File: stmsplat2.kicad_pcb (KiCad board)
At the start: 2 copper layers, 100 x 100 mm, 115 parts, among them J1 C11_2X36, J10 Conn_01x03_Male, J11 Conn_01x02_Male, J12 Conn_01x04_Male, J13 Conn_01x04_Male, J14 Conn_01x02, J15 Conn_01x02, J16 Screw_Terminal_01x03, J17 Screw_Terminal_01x02, J18 Conn_01x02_Male, J19 Conn_01x02_Male, J2 C12_2X36, J3 Conn_01x04_Male, J4 Conn_01x04_Male, J5 Conn_Coaxial, J6 Conn_01x04_Male, J7 Conn_01x04_Male, J8 Conn_01x04_Male, J9 Conn_01x03_Male, Q1 BSS138LT1G, SW1 SW_DIP_x02, U1 ublox_chinese_PCB_module, U10 XCVR_E30-400M20S (Si4463), U11 3115_module, U2 ESP-C3-13U, U3 SST25VF032B, U4 48L512-48LM01, U5 Opamp_Quad_MCP6024, U6 E180-ZG120A, U7 AZ1084C, U8 MCP6S93-X_UN, U9 DS2485

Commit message: Splat2 Revision A.  Work-in-progress
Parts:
- J1, J2: footprint Connector_Samtec_HLE_THT:Samtec_HLE-136-02-xx-DV-TE_2x36_P2.54mm_Horizontal -> Connector_PinSocket_2.54mm:PinSocket_2x36_P2.54mm_Vertical
- R7, R8: value 4K7 -> 1K
- moved TP10 2.07 mm to (149.8, 140.0)
- turned J1 to 180 degrees
- turned J2 to 180 degrees
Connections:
- net Net-(C13-Pad1) renamed /OUR3V3
- C1 pad 1: VDD -> +3V3
- C11 pad 1: +5V -> 5VEXT
- C14 pad 2: VDD -> +3V3
- C15 pad 1: VDD -> +3V3
- C16 pad 2: VDD -> +3V3
- C17 pad 2: VDD -> +3V3
- C18 pad 1: VDD -> +3V3
- C19 pad 2: VDD -> +3V3
- C2 pad 1: VDD -> +3V3
- C20 pad 1: VDD -> +3V3
- C21 pad 2: VDD -> +3V3
- C28 pad 1: VDD -> +3V3
- C3 pad 1: VDD -> +3V3
- C30 pad 1: VDD -> +3V3
- C31 pad 1: VDD -> +3V3
- FB1 pad 2: +5V -> 5VEXT
- FB2 pad 1: VDD -> +3V3
- J1 pad 16: /+3V3 -> +3V3
- J1 pad 18: +5V -> +5VSTM
- J1 pad 5: VDD -> /3V3_VPP
- J1 pad 57: /PD0 -> PD0
- J1 pad 6: +5V -> 5VEXT
- J12 pad 1: VDD -> +3V3
- J13 pad 1: VDD -> +3V3
- J19 pad 2: VDD -> +3V3
- J4 pad 1: VDD -> +3V3
- J7 pad 1: VDD -> +3V3
- Q1 pad 3: VDD -> +3V3
- R1 pad 1: VDD -> +3V3
- R10 pad 2: GNDA -> /HALF3V3
- R11 pad 1: VDD -> +3V3
- R13 pad 1: VDD -> +3V3
- R14 pad 1: VDD -> +3V3
- R16 pad 2: VDD -> +3V3
- R21 pad 1: VDD -> +3V3
- R22 pad 1: VDD -> +3V3
- R4 pad 1: VDD -> +3V3
- U1 pad 1: VDD -> +3V3
- U10 pad 9: VDD -> +3V3
- U11 pad 1: PB9 -> PD0
- U11 pad 5: VDD -> +3V3
- U2 pad 1: VDD -> +3V3
- U3 pad 8: VDD -> +3V3
- U4 pad 8: VDD -> +3V3
- U6 pad 3: VDD -> +3V3
- U7 pad 3: +5V -> 5VEXT
- U9 pad 6: VDD -> +3V3
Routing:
- net +3V3: track 0.00 -> 574.4 mm, vias 0 -> 8
- net VDD: track 569.9 -> 0.00 mm, vias 8 -> 0
- net PA4: track 153.4 -> 0.00 mm, vias 3 -> 0
- net PE6: track 131.7 -> 0.00 mm, vias 5 -> 0
- net PC10: track 125.1 -> 0.00 mm, vias 6 -> 0
- net PA0: track 126.4 -> 8.97 mm, vias 2 -> 1
- net PD11: track 115.9 -> 0.00 mm, vias 3 -> 0
- net PC6: track 115.7 -> 0.00 mm, vias 1 -> 0
- net PE1: track 115.0 -> 0.00 mm, vias 1 -> 0
- net PE2: track 114.8 -> 0.00 mm, vias 5 -> 0
- net PB9: track 109.7 -> 0.00 mm, vias 3 -> 0
- net PE13: track 109.0 -> 0.00 mm, vias 4 -> 0
- net PG9: track 107.6 -> 0.00 mm, vias 2 -> 0
- net PF2: track 100.8 -> 0.00 mm, vias 3 -> 0
- net PG2: track 99.4 -> 0.00 mm, vias 3 -> 0
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- removed copper zone on B.Cu, net GND
- removed copper zone on B.Cu, net GNDA
- removed copper zone on F.Cu, net GNDA
- removed copper zone on F.Cu, net VDD
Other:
- board text added: "1"
- board text added: "1W"
- board text added: "3V3"
- board text added: "5VIN"
- board text added: "COM2"
- board text added: "COM7"
- board text added: "I2C2"
- board text added: "INT3V"
- board text added: "RST"
- board text added: "SPLAT2 DEVELOPMENT BOARD Rev A"
- board text added: "SPLAT2 RevA bdars.org.au"
- board text removed: "B/OUT"
- board text removed: "COM"
- board text removed: "DCOM"
- board text removed: "I2C"
- board text removed: "SPLAT2 DEVELOPMENT BOARD V1 .0"
- board text removed: "SPLAT2 v1.0 bdars.org.au"

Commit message: Routed but needs checking
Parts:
- added J20: Conn_01x02_Male, Connector_PinHeader_2.54mm:PinHeader_1x02_P2.54mm_Vertical, F.Cu at (85.8, 91.7)
- D10, D2, D3, D4, D5, D6, D7, D8, D9: footprint LED_SMD:LED_PLCC-2 -> splat2-kicad:LED_PLCC-2
- J9: value Conn_01x03_Male -> Conn_01x04_Male; footprint Connector_PinHeader_2.54mm:PinHeader_1x03_P2.54mm_Vertical -> Connector_PinHeader_2.54mm:PinHeader_1x04_P2.54mm_Vertical
- U2: footprint ESP-C3-13 -> splat2-kicad:ESP-C3-13
- moved J9 17.7 mm to (63.6, 139.8)
- renumbered J1 to CN11, J2 to CN12
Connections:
- net /PF6 renamed PF6
- CN12 pad 18: /PB11 -> PB11
- J9 pad 1: PF1 -> +3V3
- J9 pad 2: PF0 -> PF1
- J9 pad 3: GND -> PF0
- U6 pad 17: Net-(U6-Pad17) -> PB11
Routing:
- net PA4: track 0.00 -> 168.3 mm, vias 0 -> 1
- net PE13: track 0.00 -> 159.0 mm, vias 0 -> 4
- net PE6: track 0.00 -> 156.3 mm, vias 0 -> 5
- net PC6: track 0.00 -> 137.6 mm, vias 0 -> 2
- net PE5: track 0.00 -> 136.5 mm, vias 0 -> 9
- net PE2: track 0.00 -> 112.6 mm, vias 0 -> 5
- net PG9: track 0.00 -> 103.6 mm, vias 0 -> 1
- net PD12: track 0.00 -> 100.6 mm, vias 0 -> 4
- net PB9: track 0.00 -> 100.0 mm, vias 0 -> 1
- net PE1: track 0.00 -> 97.0 mm
- net PC10: track 0.00 -> 93.9 mm, vias 0 -> 2
- net PD11: track 0.00 -> 93.8 mm, vias 0 -> 3
- net PD0: track 0.00 -> 92.3 mm
- net PG2: track 0.00 -> 92.3 mm, vias 0 -> 3
- net PB12: track 0.00 -> 92.0 mm, vias 0 -> 3
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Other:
- board text added: "CN11"
- board text added: "CN12"
- board text added: "INT5V"
- board text removed: "J1"

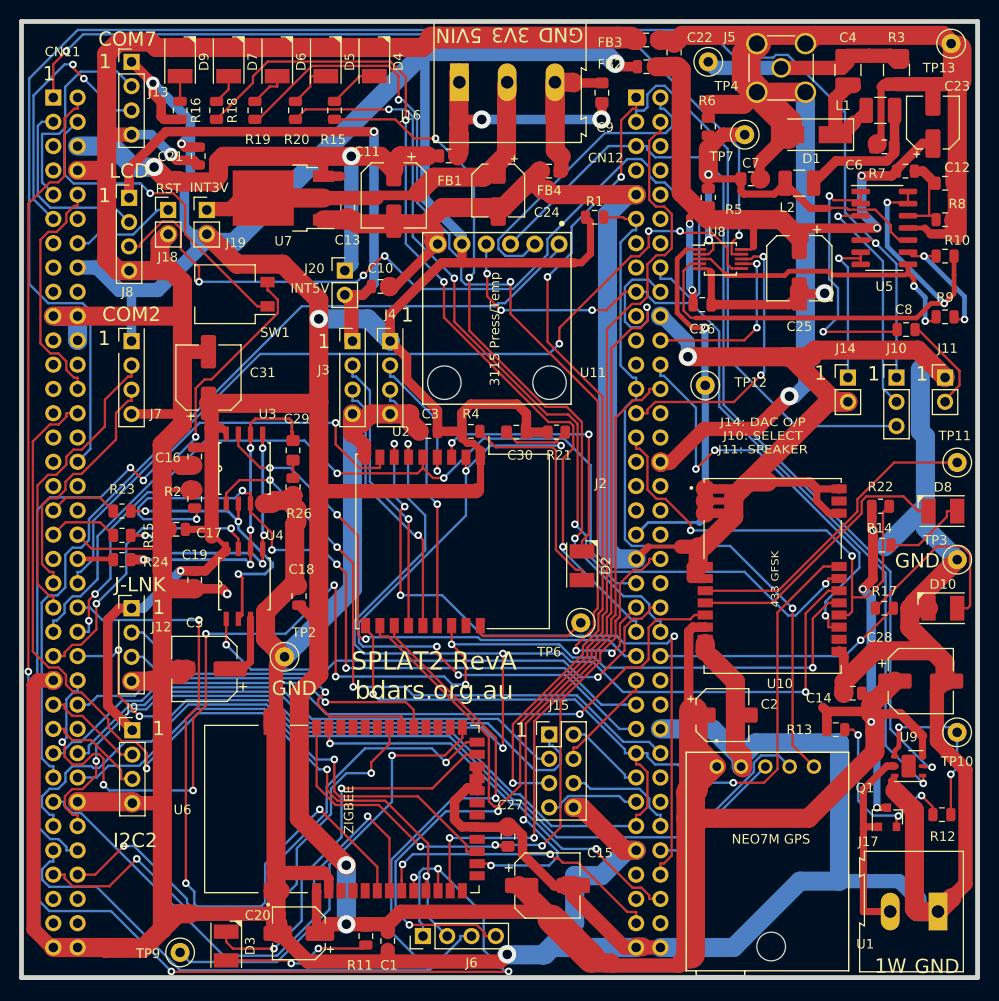
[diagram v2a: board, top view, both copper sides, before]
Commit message: Copper pours added
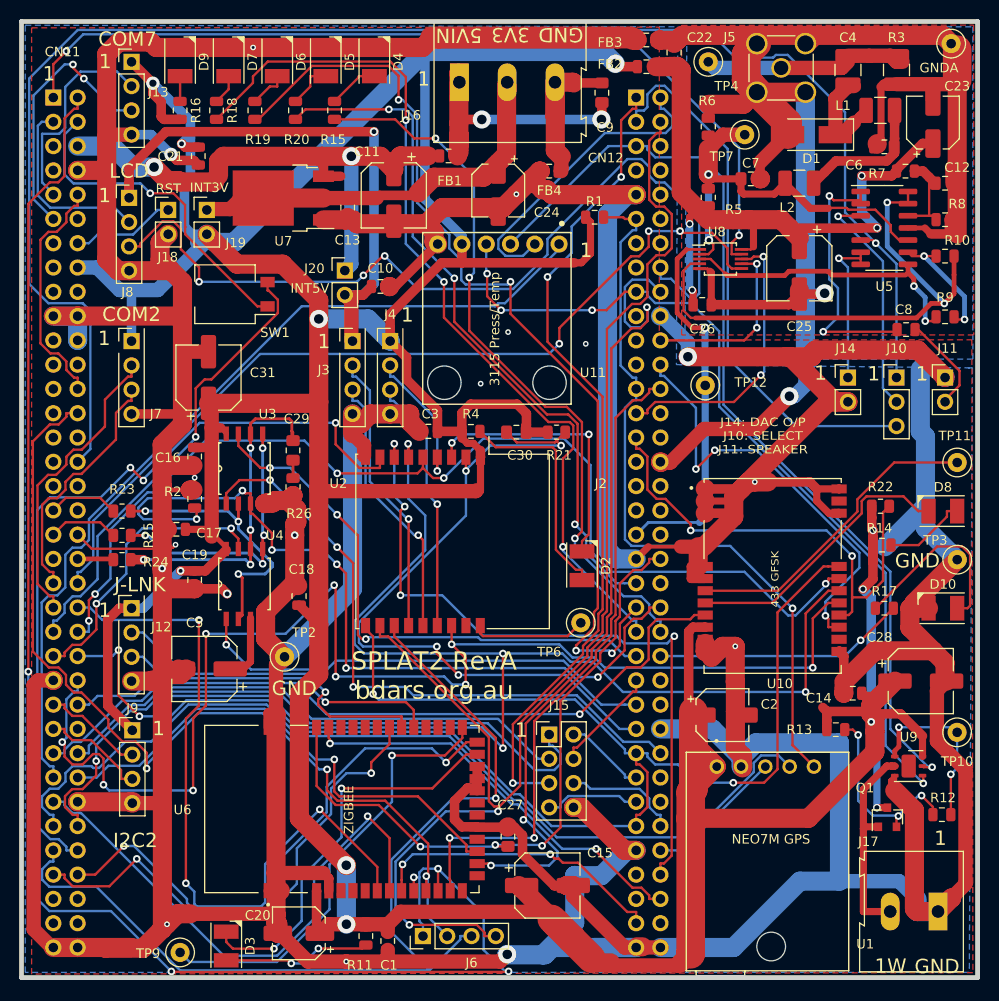
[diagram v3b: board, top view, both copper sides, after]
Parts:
- renumbered TP13 to GNDA
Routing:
- net GND: track 929.8 -> 935.9 mm, vias 4 -> 17
- added copper zone on B.Cu, net GND
- added copper zone on F.Cu, net GND
- added copper zone on B.Cu, net GNDA
- added copper zone on F.Cu, net GNDA

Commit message: Sent off for PCB manufacture
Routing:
- net /PF5: track 0.00 -> 2.00 mm
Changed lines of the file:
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@@
     (thickness 1.6)
     (drawings 47)
-    (tracks 2746)
+    (tracks 2747)
     (zones 0)
     (modules 116)
@@
   )
   (setup
-    (last_trace_width 2)
+    (last_trace_width 0.25)
     (user_trace_width 0.25)
     (user_trace_width 0.3)
@@
   (target plus (at 48.26 170.18) (size 5) (width 0.15) (layer Edge.Cuts))
   (gr_line (start 125.1 33.8) (end 125.09 33.79) (layer F.Paste) (width 0.2))
+  (segment (start 118.821 116.764) (end 120.233 118.176) (width 0.25) (layer F.Cu) (net 11))
   (segment (start 143.33 144.959) (end 143.2687 144.959) (width 0.4006) (layer F.Cu) (net 20))
   (segment (start 143.2687 144.959) (end 142.829 145.3987) (width 0.4006) (layer F.Cu) (net 20))
@@
   (segment (start 67.808 120.65) (end 68.102 120.356) (width 0.3) (layer F.Cu) (net 20))
   (segment (start 68.102 120.356) (end 68.102 120.356) (width 0.3) (layer F.Cu) (net 20))
-  (via (at 68.102 120.356) (size 0.6) (drill 0.3) (layers F.Cu B.Cu) (net 20))
+  (via (at 68.102 120.356) (size 0.8) (drill 0.4) (layers F.Cu B.Cu) (net 20))
   (segment (start 67.1345 112.062) (end 69.9305 112.062) (width 2) (layer F.Cu) (net 20))
   (segment (start 70.104 112.2355) (end 69.9305 112.062) (width 0.3) (layer F.Cu) (net 20))
   (segment (start 70.104 114.6325) (end 70.104 113.344) (width 0.3) (layer F.Cu) (net 20))
   (segment (start 70.104 113.344) (end 70.104 112.2355) (width 0.3) (layer F.Cu) (net 20))
-  (via (at 70.104 113.344) (size 0.6) (drill 0.3) (layers F.Cu B.Cu) (net 20))
+  (via (at 70.104 113.344) (size 0.8) (drill 0.4) (layers F.Cu B.Cu) (net 20))
   (segment (start 103.753277 83.698277) (end 105.346 82.1055) (width 2) (layer F.Cu) (net 20))
-  (via (at 103.753277 83.698277) (size 0.6) (drill 0.3) (layers F.Cu B.Cu) (net 20))
+  (via (at 103.753277 83.698277) (size 0.8) (drill 0.4) (layers F.Cu B.Cu) (net 20))
   (segment (start 76.22 68.35) (end 73.66 68.35) (width 2) (layer F.Cu) (net 20))
-  (via (at 76.22 68.35) (size 0.6) (drill 0.3) (layers F.Cu B.Cu) (net 20))
+  (via (at 76.22 68.35) (size 0.8) (drill 0.4) (layers F.Cu B.Cu) (net 20))
   (segment (start 67.210081 160.052081) (end 68.3029 158.959) (width 2) (layer F.Cu) (net 20))
-  (via (at 67.210081 160.052081) (size 0.6) (drill 0.3) (layers F.Cu B.Cu) (net 20))
+  (via (at 67.210081 160.052081) (size 0.8) (drill 0.4) (layers F.Cu B.Cu) (net 20))
   (segment (start 85.959 163.95) (end 90.304 163.95) (width 1.5) (layer F.Cu) (net 20))
-  (via (at 85.959 163.95) (size 0.6) (drill 0.3) (layers F.Cu B.Cu) (net 20))
+  (via (at 85.959 163.95) (size 0.8) (drill 0.4) (layers F.Cu B.Cu) (net 20))
   (segment (start 128.69 113.792) (end 130.048 113.792) (width 2) (layer F.Cu) (net 20))
-  (via (at 128.69 113.792) (size 0.6) (drill 0.3) (layers F.Cu B.Cu) (net 20))
+  (via (at 128.69 113.792) (size 1.9) (drill 1) (layers F.Cu B.Cu) (net 20))
   (segment (start 126.647 134.661) (end 126.647 130.985) (width 2) (layer F.Cu) (net 20))
   (segment (start 126.66 134.674) (end 126.647 134.661) (width 2) (layer F.Cu) (net 20))
@@
   (segment (start 126.647 130.985) (end 125.333 130.985) (width 2) (layer F.Cu) (net 20))
   (segment (start 126.647 130.985) (end 126.647 130.985) (width 2) (layer F.Cu) (net 20))
-  (via (at 126.647 130.985) (size 0.6) (drill 0.3) (layers F.Cu B.Cu) (net 20))
-  (via (at 100.016 103.511) (size 0.6) (drill 0.3) (layers F.Cu B.Cu) (net 20))
-  (via (at 102.885 98.118) (size 0.6) (drill 0.3) (layers F.Cu B.Cu) (net 20))
-  (via (at 111.013 99.345) (size 0.6) (drill 0.3) (layers F.Cu B.Cu) (net 20))
+  (via (at 126.647 130.985) (size 0.8) (drill 0.4) (layers F.Cu B.Cu) (net 20))
+  (via (at 100.016 103.511) (size 0.8) (drill 0.4) (layers F.Cu B.Cu) (net 20))
+  (via (at 102.885 98.118) (size 0.8) (drill 0.4) (layers F.Cu B.Cu) (net 20))
+  (via (at 111.013 99.345) (size 0.8) (drill 0.4) (layers F.Cu B.Cu) (net 20))
   (segment (start 75.946 128.1176) (end 75.946 128.016) (width 0.75) (layer F.Cu) (net 21))
   (segment (start 73.914 133.35) (end 75.184 133.35) (width 0.75) (layer F.Cu) (net 21))
